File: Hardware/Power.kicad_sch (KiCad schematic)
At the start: 24 parts, among them J1 Conn_01x02_Pin, J2 MP1584 Breakout, J6 Conn_01x06_Pin, J7 Conn_01x06_Pin, SW2 SW_SPDT, SW5 SW_SPDT

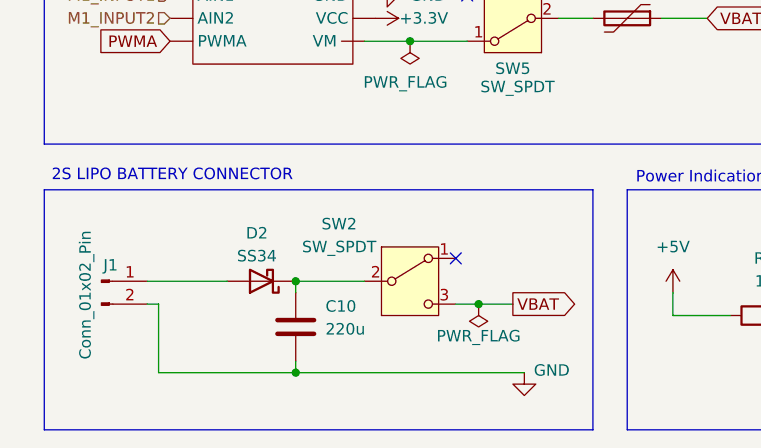
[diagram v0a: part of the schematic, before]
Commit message: Made changes with i2c bus, added state connection and removed en of hc05, added bno085 fuse,bno085 2nd 3v3 unconnected flag has been put, reversed the connection for battery connector based on the xt30 signs,removed all daisy chained power traces and made it into start topology, fiexd drc erros,dfm check erros
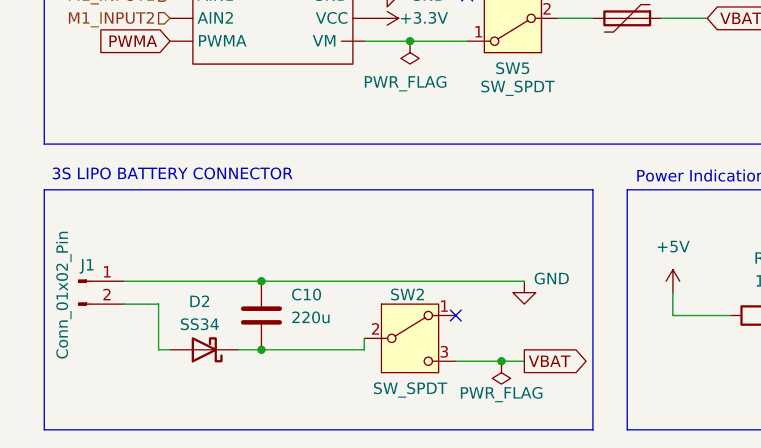
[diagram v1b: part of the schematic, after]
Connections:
- net GND: now also C10.1, J1.1 (Pin_1); no longer C10.2, J1.2 (Pin_2)
- net at D2.1 (K), SW2.2 (B): now also C10.2; no longer C10.1
- net at D2.2 (A): now also J1.2 (Pin_2); no longer J1.1 (Pin_1)
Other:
- note added: "3S LIPO BATTERY CONNECTOR"
- note removed: "2S LIPO BATTERY CONNECTOR"
- moved on the sheet: C10, D2, J1, SW2
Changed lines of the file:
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@@
 		)
 	)
-	(text "2S LIPO BATTERY CONNECTOR"
+	(text "3S LIPO BATTERY CONNECTOR"
 		(exclude_from_sim no)
 		(at 54.864 105.156 0)
@@
 	)
 	(junction
-		(at 179.07 114.3)
+		(at 64.77 124.46)
 		(diameter 0)
 		(color 0 0 0 0)
 	)
 	(junction
-		(at 68.58 116.84)
+		(at 179.07 114.3)
 		(diameter 0)
 		(color 0 0 0 0)
 	)
 	(junction
-		(at 68.58 127)
+		(at 64.77 116.84)
 		(diameter 0)
 		(color 0 0 0 0)
@@
 	)
 	(junction
-		(at 88.9 119.38)
+		(at 81.28 90.17)
 		(diameter 0)
 		(color 0 0 0 0)
 	)
 	(junction
-		(at 81.28 90.17)
+		(at 91.44 125.73)
 		(diameter 0)
 		(color 0 0 0 0)
@@
 	)
 	(no_connect
-		(at 86.36 114.3)
+		(at 86.36 120.65)
 	)
 	(wire
@@
 	(wire
 		(pts
+			(xy 91.44 125.73) (xy 93.98 125.73)
+		)
+		(stroke
+			(width 0)
+			(type default)
+		)
+	)
+	(wire
+		(pts
 			(xy 219.71 116.84) (xy 218.44 116.84)
 		)
@@
 	(wire
 		(pts
-			(xy 68.58 116.84) (xy 68.58 118.11)
+			(xy 218.44 114.3) (xy 223.52 114.3)
 		)
 		(stroke
@@
 	(wire
 		(pts
-			(xy 218.44 114.3) (xy 223.52 114.3)
+			(xy 64.77 116.84) (xy 93.98 116.84)
 		)
 		(stroke
@@
 	(wire
 		(pts
-			(xy 88.9 119.38) (xy 92.71 119.38)
+			(xy 110.49 120.65) (xy 116.84 120.65)
 		)
 		(stroke
@@
 	(wire
 		(pts
-			(xy 110.49 120.65) (xy 116.84 120.65)
+			(xy 76.2 124.46) (xy 76.2 123.19)
 		)
 		(stroke
@@
 	(wire
 		(pts
-			(xy 53.34 127) (xy 68.58 127)
+			(xy 179.07 109.22) (xy 179.07 114.3)
 		)
 		(stroke
@@
 	(wire
 		(pts
-			(xy 179.07 109.22) (xy 179.07 114.3)
+			(xy 179.07 127) (xy 179.07 124.46)
 		)
 		(stroke
@@
 	(wire
 		(pts
-			(xy 179.07 127) (xy 179.07 124.46)
+			(xy 205.74 132.08) (xy 205.74 127)
 		)
 		(stroke
@@
 	(wire
 		(pts
-			(xy 205.74 132.08) (xy 205.74 127)
+			(xy 53.34 124.46) (xy 54.61 124.46)
 		)
 		(stroke
@@
 	(wire
 		(pts
-			(xy 166.37 109.22) (xy 179.07 109.22)
+			(xy 62.23 124.46) (xy 64.77 124.46)
 		)
 		(stroke
@@
 	(wire
 		(pts
-			(xy 53.34 127) (xy 53.34 119.38)
+			(xy 166.37 109.22) (xy 179.07 109.22)
 		)
 		(stroke
@@
 	(wire
 		(pts
-			(xy 52.07 116.84) (xy 60.96 116.84)
+			(xy 49.53 116.84) (xy 64.77 116.84)
 		)
 		(stroke
@@
 	(wire
 		(pts
-			(xy 68.58 127) (xy 93.98 127)
+			(xy 76.2 90.17) (xy 81.28 90.17)
 		)
 		(stroke
@@
 	(wire
 		(pts
-			(xy 76.2 90.17) (xy 81.28 90.17)
+			(xy 53.34 119.38) (xy 53.34 124.46)
 		)
 		(stroke
@@
 	(wire
 		(pts
-			(xy 53.34 119.38) (xy 52.07 119.38)
+			(xy 53.34 119.38) (xy 49.53 119.38)
 		)
 		(stroke
@@
 	(wire
 		(pts
-			(xy 86.36 119.38) (xy 88.9 119.38)
+			(xy 86.36 125.73) (xy 91.44 125.73)
 		)
 		(stroke
@@
 	(wire
 		(pts
-			(xy 68.58 116.84) (xy 76.2 116.84)
-		)
-		(stroke
-			(width 0)
-			(type default)
-		)
-	)
-	(wire
-		(pts
-			(xy 68.58 125.73) (xy 68.58 127)
+			(xy 64.77 124.46) (xy 76.2 124.46)
 		)
 		(stroke
@@
 	(global_label "VBAT"
 		(shape output)
-		(at 92.71 119.38 0)
+		(at 93.98 125.73 0)
 		(fields_autoplaced yes)
 		(effects
@@
 		)
 		(property "Intersheetrefs" "${INTERSHEET_REFS}"
-			(at 100.11 119.38 0)
+			(at 101.38 125.73 0)
 			(hide yes)
 			(show_name no)
@@
 	(symbol
 		(lib_id "Device:C")
-		(at 68.58 121.92 0)
+		(at 64.77 120.65 0)
 		(unit 1)
 		(body_style 1)
@@
 		(dnp no)
 		(property "Reference" "C10"
-			(at 71.882 119.634 0)
+			(at 68.072 118.364 0)
 			(show_name no)
 			(do_not_autoplace no)
@@
 		)
 		(property "Value" "220u"
-			(at 71.882 122.174 0)
+			(at 68.072 120.904 0)
 			(show_name no)
 			(do_not_autoplace no)
@@
 		)
 		(property "Footprint" "Capacitor_THT:CP_Radial_D6.3mm_P2.50mm"
-			(at 69.5452 125.73 0)
+			(at 65.7352 124.46 0)
 			(hide yes)
 			(show_name no)
@@
 		)
 		(property "Datasheet" ""
-			(at 68.58 121.92 0)
+			(at 64.77 120.65 0)
 			(hide yes)
 			(show_name no)
@@
 		)
 		(property "Description" "Unpolarized capacitor"
-			(at 68.58 121.92 0)
+			(at 64.77 120.65 0)
 			(hide yes)
 			(show_name no)
@@
 	(symbol
 		(lib_id "Switch:SW_SPDT")
-		(at 81.28 116.84 0)
+		(at 81.28 123.19 0)
 		(unit 1)
 		(body_style 1)
@@
 		(dnp no)
 		(property "Reference" "SW2"
-			(at 73.406 110.49 0)
+			(at 81.026 118.364 0)
 			(show_name no)
 			(do_not_autoplace no)
@@
 		)
 		(property "Value" "SW_SPDT"
-			(at 73.406 113.03 0)
+			(at 81.28 128.778 0)
 			(show_name no)
 			(do_not_autoplace no)
@@
 		)
 		(property "Footprint" "Button_Switch_THT:SW_Slide_SPDT_Angled_CK_OS102011MA1Q"
-			(at 81.28 116.84 0)
+			(at 81.28 123.19 0)
 			(hide yes)
 			(show_name no)
@@
 		)
 		(property "Datasheet" ""
-			(at 81.28 124.46 0)
+			(at 81.28 130.81 0)
 			(hide yes)
 			(show_name no)
@@
 		)
 		(property "Description" "Switch, single pole double throw"
-			(at 81.28 116.84 0)
+			(at 81.28 123.19 0)
 			(hide yes)
 			(show_name no)
@@
 	(symbol
 		(lib_id "Diode:SS34")
-		(at 64.77 116.84 180)
+		(at 58.42 124.46 180)
 		(unit 1)
 		(body_style 1)
@@
 		(dnp no)
 		(property "Reference" "D2"
-			(at 64.262 111.506 0)
+			(at 57.912 119.126 0)
 			(show_name no)
 			(do_not_autoplace no)
@@
 		)
 		(property "Value" "SS34"
-			(at 64.262 114.046 0)
+			(at 57.912 121.666 0)
 			(show_name no)
 			(do_not_autoplace no)
@@
 		)
 		(property "Footprint" "Diode_SMD:D_SMA_Handsoldering"
-			(at 64.77 112.395 0)
+			(at 58.42 120.015 0)
 			(hide yes)
 			(show_name no)
@@
 		)
 		(property "Datasheet" "https://www.vishay.com/docs/88751/ss32.pdf"
-			(at 64.77 116.84 0)
+			(at 58.42 124.46 0)
 			(hide yes)
 			(show_name no)
@@
 		)
 		(property "Description" "40V 3A Schottky Diode, SMA"
-			(at 64.77 116.84 0)
+			(at 58.42 124.46 0)
 			(hide yes)
 			(show_name no)
@@
 	(symbol
 		(lib_id "power:GND")
-		(at 93.98 127 0)
+		(at 93.98 116.84 0)
 		(unit 1)
 		(body_style 1)
@@
 		(dnp no)
 		(property "Reference" "#PWR01"
-			(at 93.98 133.35 0)
+			(at 93.98 123.19 0)
 			(hide yes)
 			(show_name no)
@@
 		)
 		(property "Value" "GND"
-			(at 97.028 126.746 0)
+			(at 97.028 116.586 0)
 			(show_name no)
 			(do_not_autoplace no)
@@
 		)
 		(property "Footprint" ""
-			(at 93.98 127 0)
+			(at 93.98 116.84 0)
 			(hide yes)
 			(show_name no)
@@
 		)
 		(property "Datasheet" ""
-			(at 93.98 127 0)
+			(at 93.98 116.84 0)
 			(hide yes)
 			(show_name no)
@@
 		)
 		(property "Description" "Power symbol creates a global label with name \"GND\" , ground"
-			(at 93.98 127 0)
+			(at 93.98 116.84 0)
 			(hide yes)
 			(show_name no)
@@
 	(symbol
 		(lib_id "Connector:Conn_01x02_Pin")
-		(at 46.99 116.84 0)
+		(at 44.45 116.84 0)
 		(unit 1)
 		(body_style 1)
@@
 		(dnp no)
 		(property "Reference" "J1"
-			(at 48.006 115.062 0)
+			(at 45.466 115.062 0)
 			(show_name no)
 			(do_not_autoplace no)
@@
 		)
 		(property "Value" "Conn_01x02_Pin"
-			(at 45.212 118.364 90)
+			(at 42.672 118.364 90)
 			(show_name no)
 			(do_not_autoplace no)
@@
 		)
 		(property "Footprint" "Connector_AMASS:AMASS_XT30UPB-M_1x02_P5.0mm_Vertical"
-			(at 46.99 116.84 0)
+			(at 44.45 116.84 0)
 			(hide yes)
 			(show_name no)
@@
 		)
 		(property "Datasheet" ""
-			(at 46.99 116.84 0)
+			(at 44.45 116.84 0)
 			(hide yes)
 			(show_name no)
@@
 		)
 		(property "Description" "Generic connector, single row, 01x02, script generated"
-			(at 46.99 116.84 0)
+			(at 44.45 116.84 0)
 			(hide yes)
 			(show_name no)
@@
 	(symbol
 		(lib_id "power:PWR_FLAG")
-		(at 88.9 119.38 180)
+		(at 91.44 125.73 180)
 		(unit 1)
 		(body_style 1)
@@
 		(dnp no)
 		(property "Reference" "#FLG02"
-			(at 88.9 121.285 0)
+			(at 91.44 127.635 0)
 			(hide yes)
 			(show_name no)
@@
 		)
 		(property "Value" "PWR_FLAG"
-			(at 88.9 122.936 0)
+			(at 91.44 129.286 0)
 			(show_name no)
 			(do_not_autoplace no)
@@
 		)
 		(property "Footprint" ""
-			(at 88.9 119.38 0)
+			(at 91.44 125.73 0)
 			(hide yes)
 			(show_name no)
@@
 		)
 		(property "Datasheet" ""
-			(at 88.9 119.38 0)
+			(at 91.44 125.73 0)
 			(hide yes)
 			(show_name no)
@@
 		)
 		(property "Description" "Special symbol for telling ERC where power comes from"
-			(at 88.9 119.38 0)
+			(at 91.44 125.73 0)
 			(hide yes)
 			(show_name no)
